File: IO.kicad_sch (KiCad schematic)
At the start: 7 parts

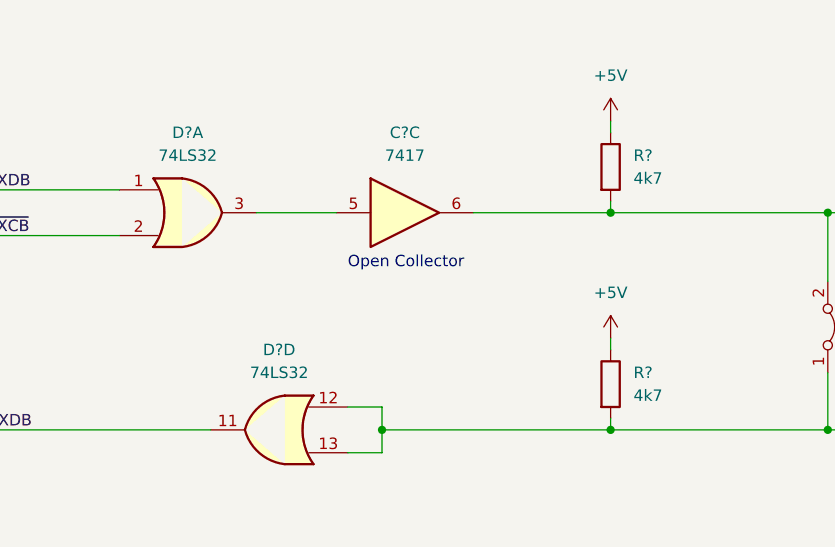
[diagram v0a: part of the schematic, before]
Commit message: Recovered IO component numbering lost in old commit
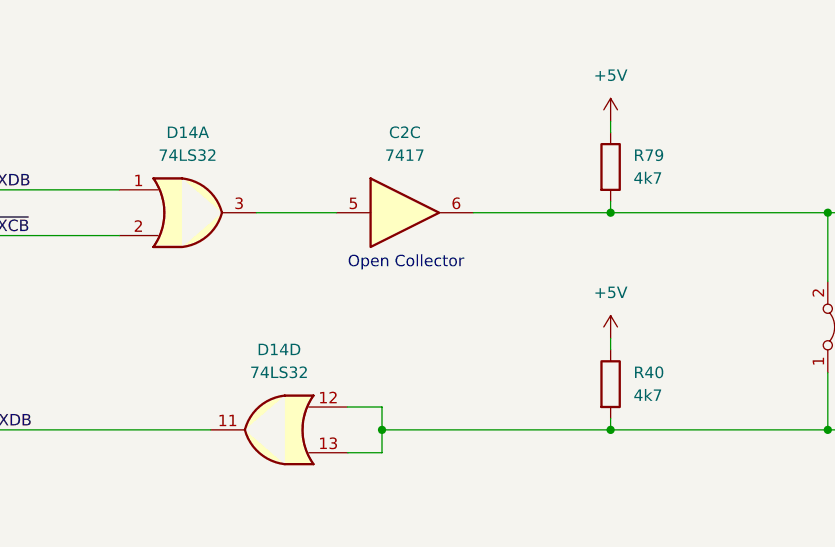
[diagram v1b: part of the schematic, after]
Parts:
- gave numbers to parts that had none: 4
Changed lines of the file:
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@@
   (symbol (lib_id "74xx:74LS32") (at 80.01 80.01 0) (mirror y) (unit 4)
     (in_bom yes) (on_board yes) (fields_autoplaced)
-    (property "Reference" "D?" (id 0) (at 80.01 71.12 0))
+    (property "Reference" "D14" (id 0) (at 80.01 71.12 0))
     (property "Value" "74LS32" (id 1) (at 80.01 73.66 0))
     (property "Footprint" "" (id 2) (at 80.01 80.01 0)
@@
   (symbol (lib_id "Device:R") (at 116.84 74.93 0) (unit 1)
     (in_bom yes) (on_board yes) (fields_autoplaced)
-    (property "Reference" "R?" (id 0) (at 119.38 73.6599 0)
+    (property "Reference" "R40" (id 0) (at 119.38 73.6599 0)
       (effects (font (size 1.27 1.27)) (justify left))
     )
@@
   (symbol (lib_id "74xx:74LS32") (at 69.85 55.88 0) (unit 1)
     (in_bom yes) (on_board yes) (fields_autoplaced)
-    (property "Reference" "D?" (id 0) (at 69.85 46.99 0))
+    (property "Reference" "D14" (id 0) (at 69.85 46.99 0))
     (property "Value" "74LS32" (id 1) (at 69.85 49.53 0))
     (property "Footprint" "" (id 2) (at 69.85 55.88 0)
@@
   (symbol (lib_id "Device:R") (at 116.84 50.8 0) (unit 1)
     (in_bom yes) (on_board yes) (fields_autoplaced)
-    (property "Reference" "R?" (id 0) (at 119.38 49.5299 0)
+    (property "Reference" "R79" (id 0) (at 119.38 49.5299 0)
       (effects (font (size 1.27 1.27)) (justify left))
     )
@@
   (symbol (lib_id "74xx:74LS07") (at 93.98 55.88 0) (unit 3)
     (in_bom yes) (on_board yes) (fields_autoplaced)
-    (property "Reference" "C?" (id 0) (at 93.98 46.99 0))
+    (property "Reference" "C2" (id 0) (at 93.98 46.99 0))
     (property "Value" "7417" (id 1) (at 93.98 49.53 0))
     (property "Footprint" "" (id 2) (at 93.98 55.88 0)

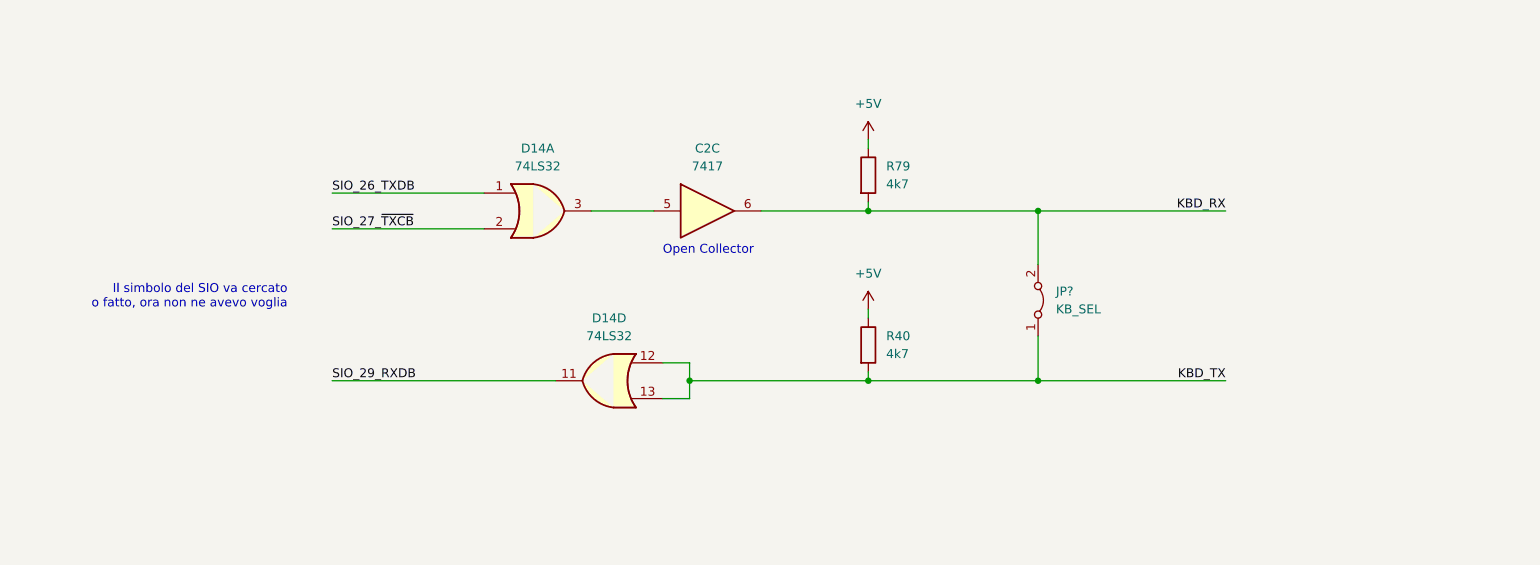
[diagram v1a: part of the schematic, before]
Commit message: Added SIO in schematics
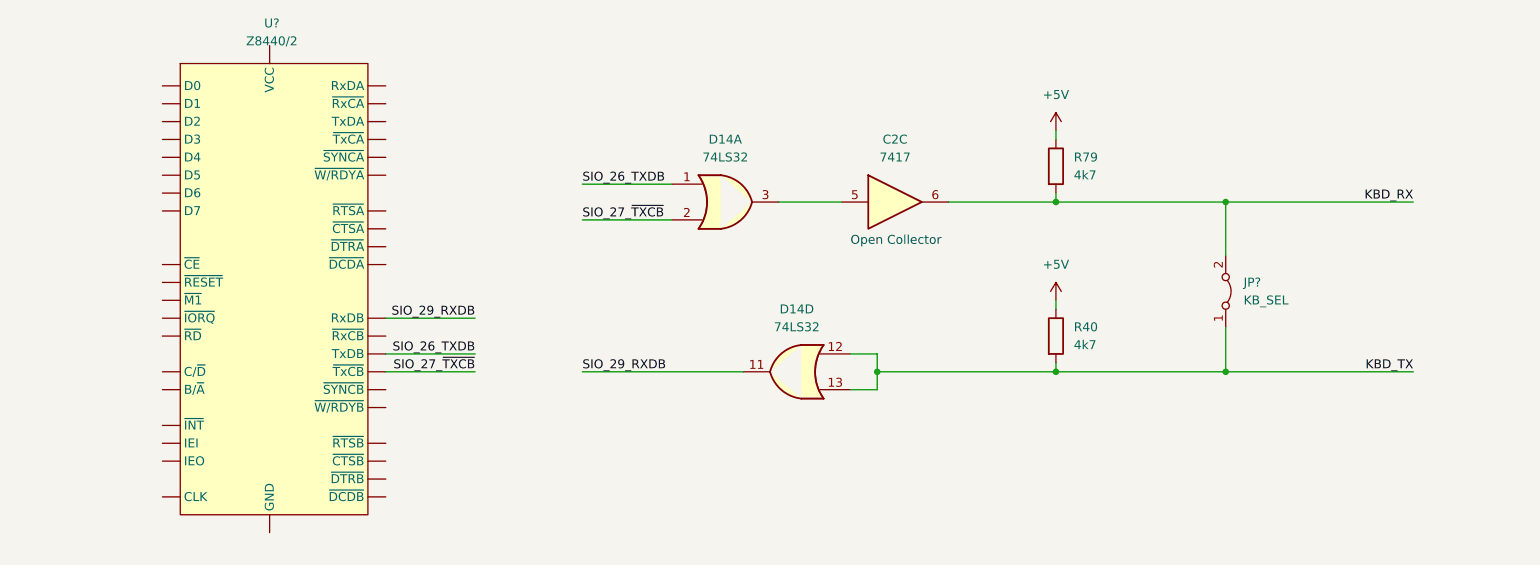
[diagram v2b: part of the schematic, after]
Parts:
- added U?: Z8440/2, symbol ceda:Z8440/2
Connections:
- net SIO_26_TXDB: now also U?. (~{W/RDYB})
- net SIO_27_~{TXCB}: now also U?. (~{W/RDYB})
- net SIO_29_RXDB: now also U?. (~{W/RDYB})
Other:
- note removed: "Il simbolo del SIO va cercato o fatto, ora non ne avevo voglia"
- moved on the sheet: C2C, D14A, D14D, JP?, R40, R79

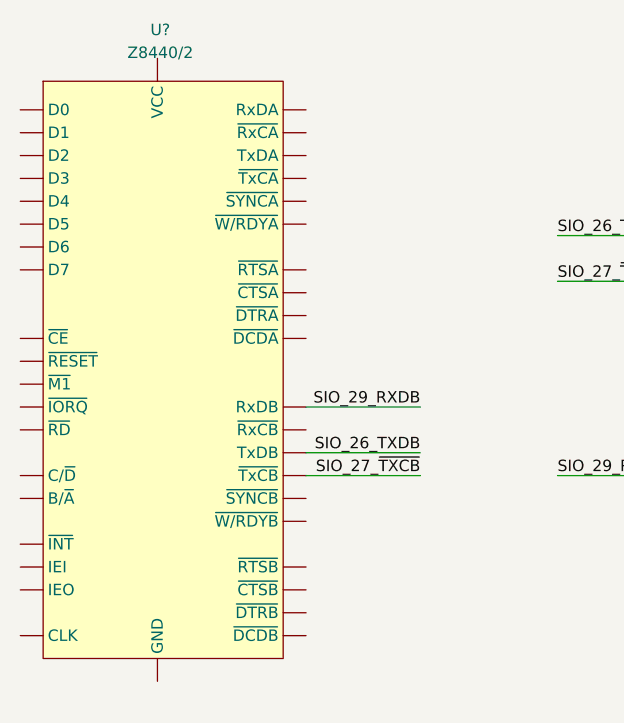
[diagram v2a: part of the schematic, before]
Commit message: Fixed SIO reference in schematic
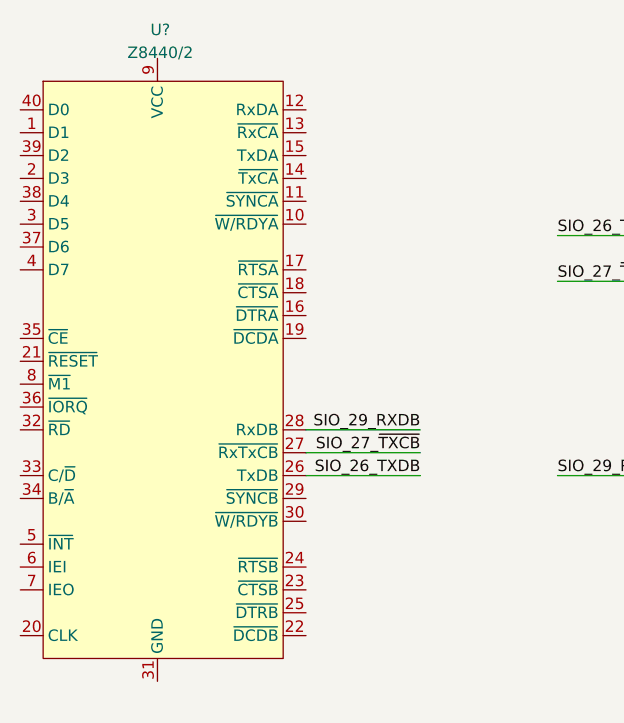
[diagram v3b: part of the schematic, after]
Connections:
- net SIO_26_TXDB: now also U?.26 (TxDB); no longer U?. (~{W/RDYB})
- net SIO_27_~{TXCB}: now also U?.27 (~{RxTxCB}); no longer U?. (~{W/RDYB})
- net SIO_29_RXDB: now also U?.28 (RxDB); no longer U?. (~{W/RDYB})
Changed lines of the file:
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@@
+    (stroke (width 0) (type default) (color 0 0 0 0))
+  )
+  (wire (pts (xy 48.26 78.74) (xy 60.96 78.74))
+    (stroke (width 0) (type default) (color 0 0 0 0))
+  )
+  (wire (pts (xy 76.2 78.74) (xy 99.06 78.74))
+    (stroke (width 0) (type default) (color 0 0 0 0))
+  )
+  (wire (pts (xy 232.41 41.91) (xy 238.76 41.91))
+    (stroke (width 0) (type default) (color 0 0 0 0))
+  )
+  (wire (pts (xy 118.11 78.74) (xy 118.11 76.2))
+    (stroke (width 0) (type default) (color 0 0 0 0))
+  )
+  (wire (pts (xy 114.3 81.28) (xy 118.11 81.28))
+    (stroke (width 0) (type default) (color 0 0 0 0))
+  )
+  (wire (pts (xy 48.26 73.66) (xy 60.96 73.66))
+    (stroke (width 0) (type default) (color 0 0 0 0))
+  )
+  (wire (pts (xy 143.51 68.58) (xy 143.51 69.85))
+    (stroke (width 0) (type default) (color 0 0 0 0))
+  )
+  (wire (pts (xy 76.2 57.15) (xy 88.9 57.15))
+    (stroke (width 0) (type default) (color 0 0 0 0))
+  )
+  (wire (pts (xy 143.51 53.34) (xy 143.51 54.61))
+    (stroke (width 0) (type default) (color 0 0 0 0))
+  )
+  (wire (pts (xy 232.41 44.45) (xy 238.76 44.45))
+    (stroke (width 0) (type default) (color 0 0 0 0))
+  )
+  (wire (pts (xy 251.46 69.85) (xy 260.35 69.85))
+    (stroke (width 0) (type default) (color 0 0 0 0))
+  )
+  (wire (pts (xy 143.51 44.45) (xy 143.51 45.72))
+    (stroke (width 0) (type default) (color 0 0 0 0))
+  )
+  (wire (pts (xy 194.31 54.61) (xy 167.64 54.61))
+    (stroke (width 0) (type default) (color 0 0 0 0))
+  )
+  (wire (pts (xy 104.14 54.61) (xy 113.03 54.61))
+    (stroke (width 0) (type default) (color 0 0 0 0))
+  )
+  (wire (pts (xy 167.64 62.23) (xy 167.64 54.61))
+    (stroke (width 0) (type default) (color 0 0 0 0))
+  )
+  (wire (pts (xy 167.64 78.74) (xy 194.31 78.74))
+    (stroke (width 0) (type default) (color 0 0 0 0))
+  )
+  (wire (pts (xy 128.27 54.61) (xy 143.51 54.61))
+    (stroke (width 0) (type default) (color 0 0 0 0))
+  )
+  (wire (pts (xy 251.46 44.45) (xy 257.81 44.45))
+    (stroke (width 0) (type default) (color 0 0 0 0))
+  )
+  (wire (pts (xy 167.64 72.39) (xy 167.64 78.74))
+    (stroke (width 0) (type default) (color 0 0 0 0))
+  )
+  (wire (pts (xy 251.46 41.91) (xy 257.81 41.91))
+    (stroke (width 0) (type default) (color 0 0 0 0))
+  )
+  (wire (pts (xy 118.11 81.28) (xy 118.11 78.74))
+    (stroke (width 0) (type default) (color 0 0 0 0))
+  )
+  (wire (pts (xy 118.11 76.2) (xy 114.3 76.2))
     (stroke (width 0) (type default) (color 0 0 0 0))
   )
   (wire (pts (xy 48.26 76.2) (xy 60.96 76.2))
-    (stroke (width 0) (type default) (color 0 0 0 0))
-  )
-  (wire (pts (xy 76.2 78.74) (xy 99.06 78.74))
-    (stroke (width 0) (type default) (color 0 0 0 0))
-  )
-  (wire (pts (xy 232.41 41.91) (xy 238.76 41.91))
-    (stroke (width 0) (type default) (color 0 0 0 0))
-  )
-  (wire (pts (xy 118.11 78.74) (xy 118.11 76.2))
-    (stroke (width 0) (type default) (color 0 0 0 0))
-  )
-  (wire (pts (xy 114.3 81.28) (xy 118.11 81.28))
-    (stroke (width 0) (type default) (color 0 0 0 0))
-  )
-  (wire (pts (xy 48.26 71.12) (xy 60.96 71.12))
-    (stroke (width 0) (type default) (color 0 0 0 0))
-  )
-  (wire (pts (xy 143.51 68.58) (xy 143.51 69.85))
-    (stroke (width 0) (type default) (color 0 0 0 0))
-  )
-  (wire (pts (xy 76.2 57.15) (xy 88.9 57.15))
-    (stroke (width 0) (type default) (color 0 0 0 0))
-  )
-  (wire (pts (xy 143.51 53.34) (xy 143.51 54.61))
-    (stroke (width 0) (type default) (color 0 0 0 0))
-  )
-  (wire (pts (xy 232.41 44.45) (xy 238.76 44.45))
-    (stroke (width 0) (type default) (color 0 0 0 0))
-  )
-  (wire (pts (xy 251.46 69.85) (xy 260.35 69.85))
-    (stroke (width 0) (type default) (color 0 0 0 0))
-  )
-  (wire (pts (xy 143.51 44.45) (xy 143.51 45.72))
-    (stroke (width 0) (type default) (color 0 0 0 0))
-  )
-  (wire (pts (xy 194.31 54.61) (xy 167.64 54.61))
-    (stroke (width 0) (type default) (color 0 0 0 0))
-  )
-  (wire (pts (xy 104.14 54.61) (xy 113.03 54.61))
-    (stroke (width 0) (type default) (color 0 0 0 0))
-  )
-  (wire (pts (xy 167.64 62.23) (xy 167.64 54.61))
-    (stroke (width 0) (type default) (color 0 0 0 0))
-  )
-  (wire (pts (xy 167.64 78.74) (xy 194.31 78.74))
-    (stroke (width 0) (type default) (color 0 0 0 0))
-  )
-  (wire (pts (xy 128.27 54.61) (xy 143.51 54.61))
-    (stroke (width 0) (type default) (color 0 0 0 0))
-  )
-  (wire (pts (xy 251.46 44.45) (xy 257.81 44.45))
-    (stroke (width 0) (type default) (color 0 0 0 0))
-  )
-  (wire (pts (xy 167.64 72.39) (xy 167.64 78.74))
-    (stroke (width 0) (type default) (color 0 0 0 0))
-  )
-  (wire (pts (xy 251.46 41.91) (xy 257.81 41.91))
-    (stroke (width 0) (type default) (color 0 0 0 0))
-  )
-  (wire (pts (xy 118.11 81.28) (xy 118.11 78.74))
-    (stroke (width 0) (type default) (color 0 0 0 0))
-  )
-  (wire (pts (xy 118.11 76.2) (xy 114.3 76.2))
-    (stroke (width 0) (type default) (color 0 0 0 0))
-  )
-  (wire (pts (xy 48.26 78.74) (xy 60.96 78.74))
     (stroke (width 0) (type default) (color 0 0 0 0))
   )
@@
     (effects (font (size 1.27 1.27)) (justify right bottom))
   )
-  (label "SIO_29_RXDB" (at 60.96 71.12 180)
+  (label "SIO_29_RXDB" (at 60.96 73.66 180)
     (effects (font (size 1.27 1.27)) (justify right bottom))
   )
@@
     (effects (font (size 1.27 1.27)) (justify left bottom))
   )
-  (label "SIO_26_TXDB" (at 60.96 76.2 180)
-    (effects (font (size 1.27 1.27)) (justify right bottom))
-  )
-  (label "SIO_27_~{TXCB}" (at 60.96 78.74 180)
+  (label "SIO_26_TXDB" (at 60.96 78.74 180)
+    (effects (font (size 1.27 1.27)) (justify right bottom))
+  )
+  (label "SIO_27_~{TXCB}" (at 60.96 76.2 180)
     (effects (font (size 1.27 1.27)) (justify right bottom))
   )
@@
       (effects (font (size 1.27 1.27)) hide)
     )
-    (pin "")
-    (pin "")
-    (pin "")
-    (pin "")
-    (pin "")
-    (pin "")
-    (pin "")
-    (pin "")
-    (pin "")
-    (pin "")
-    (pin "")
-    (pin "")
-    (pin "")
-    (pin "")
-    (pin "")
-    (pin "")
-    (pin "")
-    (pin "")
-    (pin "")
-    (pin "")
-    (pin "")
-    (pin "")
-    (pin "")
-    (pin "")
-    (pin "")
-    (pin "")
-    (pin "")
-    (pin "")
-    (pin "")
-    (pin "")
-    (pin "")
-    (pin "")
-    (pin "")
-    (pin "")
-    (pin "")
-    (pin "")
-    (pin "")
-    (pin "")
-    (pin "")
-    (pin "")
-    (pin "")
+    (pin "1")
+    (pin "10")
+    (pin "11")
+    (pin "12")
+    (pin "13")
+    (pin "14")
+    (pin "15")
+    (pin "16")
+    (pin "17")
+    (pin "18")
+    (pin "19")
+    (pin "2")
+    (pin "20")
+    (pin "21")
+    (pin "22")
+    (pin "23")
+    (pin "24")
+    (pin "25")
+    (pin "26")
+    (pin "27")
+    (pin "28")
+    (pin "29")
+    (pin "3")
+    (pin "30")
+    (pin "31")
+    (pin "32")
+    (pin "33")
+    (pin "34")
+    (pin "35")
+    (pin "36")
+    (pin "37")
+    (pin "38")
+    (pin "39")
+    (pin "4")
+    (pin "40")
+    (pin "5")
+    (pin "6")
+    (pin "7")
+    (pin "8")
+    (pin "9")
   )
   (symbol (lib_id "power:+5V") (at 143.51 68.58 0) (unit 1)
